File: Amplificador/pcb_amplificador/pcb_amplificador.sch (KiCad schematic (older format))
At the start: 102 parts, among them M1 FDS9934C, M2 FDS9934C, Q1 BC860, Q10 2SCR514P5, Q11 2SAR514P5, Q12 2SCR514P5, Q13 2SA1943-O_Q_, Q14 2SC5200-O_Q, Q15 2SA1943-O_Q_, Q16 2SC5200-O_Q, Q17 2SAR514P5, Q18 BC860, Q19 BC860, Q2 BC860, Q20 2SAR514P5, Q21 2SCR514P5, Q22 2SCR514P5, Q23 2SCR514P5, Q24 2SAR514P5, Q25 2SCR514P5, Q3 BC850, Q4 BC850, Q5 BC860, Q6 BC860, Q7 2SCR514P5, Q8 2SCR514P5, Q9 2SCR514P5

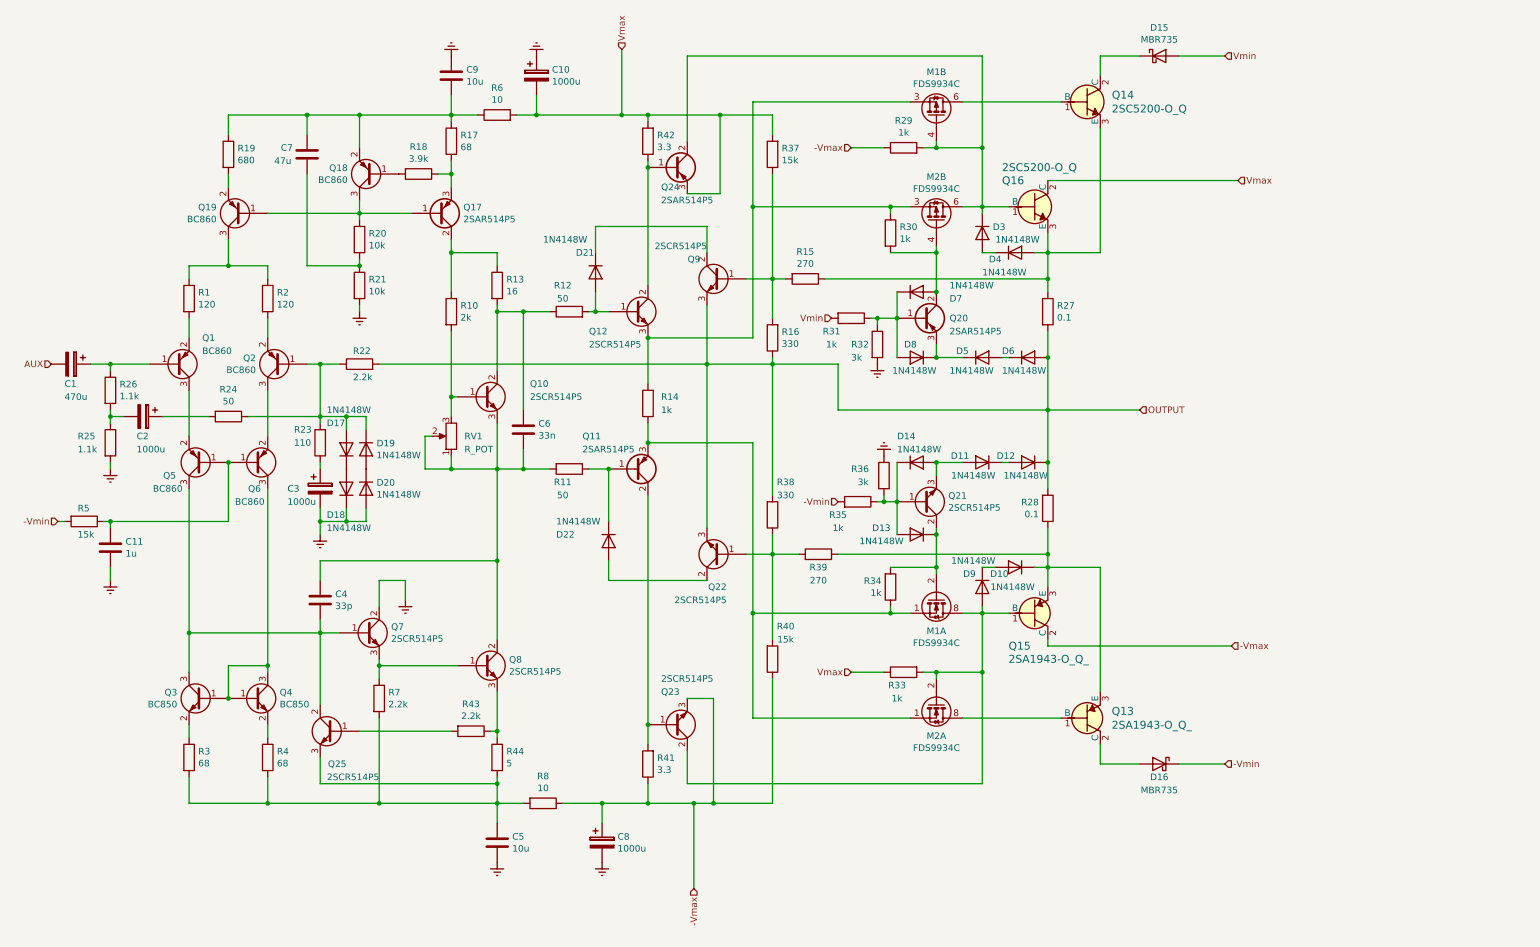
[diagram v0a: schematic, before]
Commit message: Actualizacion del esquematico del amplificador
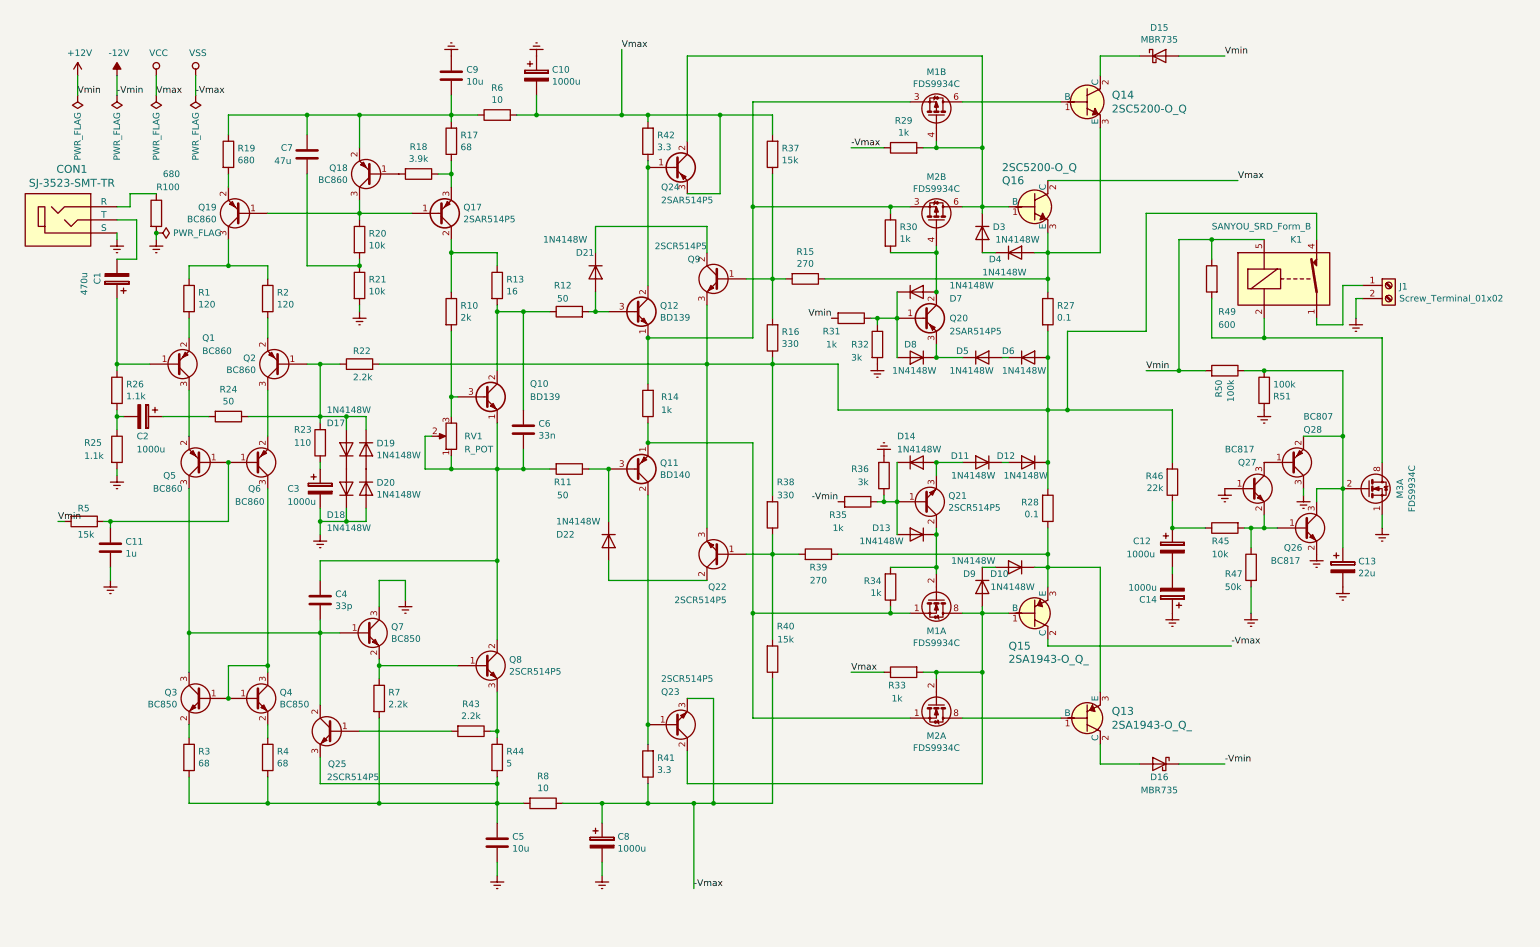
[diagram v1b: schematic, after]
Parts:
- removed Q10, Q12, Q7: 2SCR514P5, Package_TO_SOT_SMD:SOT-89-3, symbol amplificador_transistores:2SCR514P5
- removed Q11: 2SAR514P5, Package_TO_SOT_SMD:SOT-89-3, symbol amplificador_transistores:2SAR514P5
- added C12, C14: 1000u, symbol Device:CP
- added C13: 22u, symbol Device:CP
- added CON1: SJ-3523-SMT-TR, digikey-footprints:Switch_Slide_11.6x4mm_SJ-3523-SMT, symbol dk_Barrel-Audio-Connectors:SJ-3523-SMT-TR
- added J1: Screw_Terminal_01x02, symbol Connector:Screw_Terminal_01x02
- added K1: SANYOU_SRD_Form_B, Relay_THT:Relay_SPST_SANYOU_SRD_Series_Form_B, symbol Relay:SANYOU_SRD_Form_B
- added M3: FDS9934C, Package_SO:SOIC-8_3.9x4.9mm_P1.27mm, symbol Transistor_FET:FDS9934C
- added Q10, Q12: BD139, Package_TO_SOT_THT:TO-126-3_Vertical, symbol Transistor_BJT:BD139
- added Q11: BD140, Package_TO_SOT_THT:TO-126-3_Vertical, symbol Transistor_BJT:BD140
- added Q26, Q27: BC817, Package_TO_SOT_SMD:SOT-23, symbol Transistor_BJT:BC817
- added Q28: BC807, Package_TO_SOT_SMD:SOT-23, symbol Transistor_BJT:BC807
- added Q7: BC850, Package_TO_SOT_SMD:SOT-23, symbol Transistor_BJT:BC850
- added R100: 680, Resistor_SMD:R_0805_2012Metric_Pad1.15x1.40mm_HandSolder, symbol Device:R
- added R45: 10k, Resistor_SMD:R_0805_2012Metric_Pad1.15x1.40mm_HandSolder, symbol Device:R
- added R46: 22k, Resistor_SMD:R_0805_2012Metric_Pad1.15x1.40mm_HandSolder, symbol Device:R
- added R47: 50k, Resistor_SMD:R_0805_2012Metric_Pad1.15x1.40mm_HandSolder, symbol Device:R
- added R49: 600, Resistor_SMD:R_0805_2012Metric_Pad1.15x1.40mm_HandSolder, symbol Device:R
- added R50, R51: 100k, Resistor_SMD:R_0805_2012Metric_Pad1.15x1.40mm_HandSolder, symbol Device:R
- C4, C6: footprint (none) -> Capacitor_SMD:C_0805_2012Metric_Pad1.15x1.40mm_HandSolder
- R1, R10, R11, R12, R13, R14, R15, R16, R17, R18, R19, R2, R20, R22, R23, R24, R25, R26, R29, R3, R30, R31, R32, R33, R34, R35, R36, R37, R38, R39, R4, R40, R41, R42, R43, R44, R5, R6, R7, R8: footprint (none) -> Resistor_SMD:R_0805_2012Metric_Pad1.15x1.40mm_HandSolder
- R21: footprint (none) -> Resistor_SMD:R_0815_2038Metric_Pad1.53x4.00mm_HandSolder
- RV1: footprint (none) -> Potentiometer_THT:Potentiometer_Bourns_3296W_Vertical
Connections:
- net Earth: now also C13.2, C14.1, CON1.1 (S), J1.2 (Pin_2), M3.1 (S), Q26.2 (E), Q27.1 (B), Q28.3 (C), Q7.3 (C), R100.2, R47.2, R51.2
- net at C4.2, Q25.2 (C), Q3.3 (C)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: now also Q7.1 (B)
- net at Q8.1 (B), R7.1: now also Q7.2 (E)
- net at C4.1, C6.1, Q8.2 (C)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: now also Q10.1 (E)
- net at R10.2, RV1.3: now also Q10.3 (B)
- net at D22.1 (K), R11.1: now also Q11.3 (B)
- net at C6.2, R12.1, R13.2: now also Q10.2 (C)
- net at D21.2 (A), R12.2: now also Q12.3 (B)
- net at Q24.1 (B), R42.1: now also Q12.2 (C)
- net at M1.3 (1), M2.3 (1), R14.2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: now also Q12.1 (E)
- net at M1.1 (S), M2.1 (S), R14.1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: now also Q11.1 (E)
- net at Q23.1 (B), R41.2: now also Q11.2 (C)
- net -Vmax renamed VSS
- net -Vmin renamed -12V
- net -12V: no longer R5.2
- net AUX: no longer names the net of C1.2
- net AUX: now also CON1.2 (T)
- net OUTPUT: no longer names the net of D12.1 (K), D6.2 (A), Q22.3 (E), Q9.3 (E), R16.1, R22.2, R27.2, R28.2, R38.2
- net OUTPUT: now also K1.4, R46.2
- net Vmax renamed VCC
- net Vmin renamed +12V
- net +12V: now also R5.2, K1.5, R49.1, R50.2
- new net: Q26.1 (B), Q27.2 (E), R45.2, R47.1
- new net: C13.1, M3.2 (G), Q26.3 (C), Q28.2 (E), R50.1, R51.1
- new net: Q27.3 (C), Q28.1 (B)
- new net: C12.1, R45.1, R46.1
- new net: C12.2, C14.2
- new net: K1.2, M3.7 (D), M3.8 (D), R49.2
- new net: J1.1 (Pin_1), K1.1
- new net: CON1.3 (R), R100.1
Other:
- moved on the sheet: C1, R25, R26

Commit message: Actualizacion del esquematico del amplificador(2)
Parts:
- C1: value 470u -> 47u; footprint (none) -> Capacitor_SMD:CP_Elec_5x5.4
- C10, C8: footprint (none) -> Capacitor_THT:CP_Radial_D12.5mm_P5.00mm
- C11: footprint (none) -> Capacitor_SMD:C_0805_2012Metric_Pad1.15x1.40mm_HandSolder
- C12, C14: value 1000u -> 47u; footprint (none) -> Capacitor_SMD:CP_Elec_6.3x5.4
- C13: footprint (none) -> Capacitor_SMD:CP_Elec_5x5.4
- C2: value 1000u -> 470u; footprint (none) -> Capacitor_SMD:CP_Elec_10x10.5
- C3: footprint (none) -> Capacitor_SMD:CP_Elec_10x10.5
- C5, C9: footprint (none) -> Capacitor_SMD:C_1206_3216Metric_Pad1.42x1.75mm_HandSolder
- C7: footprint (none) -> Capacitor_SMD:CP_Elec_6.3x5.4
- R27, R28: footprint (none) -> Resistor_THT:R_Axial_DIN0414_L11.9mm_D4.5mm_P20.32mm_Horizontal
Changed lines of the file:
@@
 F 0 "C11" H 1315 4596 50  0000 L CNN
 F 1 "1u" H 1315 4505 50  0000 L CNN
-F 2 "" H 1238 4400 50  0001 C CNN
+F 2 "Capacitor_SMD:C_0805_2012Metric_Pad1.15x1.40mm_HandSolder" H 1238 4400 50  0001 C CNN
 F 3 "~" H 1200 4550 50  0001 C CNN
 	1    1200 4550
@@
 F 0 "C7" H 2900 1500 50  0000 R CNN
 F 1 "47u" H 2950 1600 50  0000 R CNN
-F 2 "" H 2738 1400 50  0001 C CNN
+F 2 "Capacitor_SMD:CP_Elec_6.3x5.4" H 2738 1400 50  0001 C CNN
 F 3 "~" H 2700 1550 50  0001 C CNN
 	1    2700 1550
@@
 F 0 "C5" H 4265 6846 50  0000 L CNN
 F 1 "10u" H 4265 6755 50  0000 L CNN
-F 2 "" H 4188 6650 50  0001 C CNN
+F 2 "Capacitor_SMD:C_1206_3216Metric_Pad1.42x1.75mm_HandSolder" H 4188 6650 50  0001 C CNN
 F 3 "~" H 4150 6800 50  0001 C CNN
 	1    4150 6800
@@
 F 0 "C8" H 5068 6846 50  0000 L CNN
 F 1 "1000u" H 5068 6755 50  0000 L CNN
-F 2 "" H 4988 6650 50  0001 C CNN
+F 2 "Capacitor_THT:CP_Radial_D12.5mm_P5.00mm" H 4988 6650 50  0001 C CNN
 F 3 "~" H 4950 6800 50  0001 C CNN
 	1    4950 6800
@@
 F 0 "C9" H 3685 904 50  0000 R CNN
 F 1 "10u" H 3685 995 50  0000 R CNN
-F 2 "" H 3838 800 50  0001 C CNN
+F 2 "Capacitor_SMD:C_1206_3216Metric_Pad1.42x1.75mm_HandSolder" H 3838 800 50  0001 C CNN
 F 3 "~" H 3800 950 50  0001 C CNN
 	1    3800 950
@@
 F 0 "C10" H 4568 996 50  0000 L CNN
 F 1 "1000u" H 4568 905 50  0000 L CNN
-F 2 "" H 4488 800 50  0001 C CNN
+F 2 "Capacitor_THT:CP_Radial_D12.5mm_P5.00mm" H 4488 800 50  0001 C CNN
 F 3 "~" H 4450 950 50  0001 C CNN
 	1    4450 950
@@
 F 0 "R27" H 8420 2796 50  0000 L CNN
 F 1 "0.1" H 8420 2705 50  0000 L CNN
-F 2 "" V 8280 2750 50  0001 C CNN
+F 2 "Resistor_THT:R_Axial_DIN0414_L11.9mm_D4.5mm_P20.32mm_Horizontal" V 8280 2750 50  0001 C CNN
 F 3 "~" H 8350 2750 50  0001 C CNN
 	1    8350 2750
@@
 F 0 "R28" H 8281 4204 50  0000 R CNN
 F 1 "0.1" H 8281 4295 50  0000 R CNN
-F 2 "" V 8280 4250 50  0001 C CNN
+F 2 "Resistor_THT:R_Axial_DIN0414_L11.9mm_D4.5mm_P20.32mm_Horizontal" V 8280 4250 50  0001 C CNN
 F 3 "~" H 8350 4250 50  0001 C CNN
 	1    8350 4250
@@
 F 0 "C3" H 2550 4100 50  0000 L CNN
 F 1 "1000u" H 2550 4000 50  0000 L CNN
-F 2 "" H 2838 3950 50  0001 C CNN
+F 2 "Capacitor_SMD:CP_Elec_10x10.5" H 2838 3950 50  0001 C CNN
 F 3 "~" H 2800 4100 50  0001 C CNN
 	1    2800 4100
@@
 P 1450 3550
 F 0 "C2" V 1600 3500 50  0000 L CNN
-F 1 "1000u" V 1700 3500 50  0000 L CNN
-F 2 "" H 1488 3400 50  0001 C CNN
+F 1 "470u" V 1700 3500 50  0000 L CNN
+F 2 "Capacitor_SMD:CP_Elec_10x10.5" H 1488 3400 50  0001 C CNN
 F 3 "~" H 1450 3550 50  0001 C CNN
 	1    1450 3550
@@
 P 1250 2500
 F 0 "C1" V 1400 2450 50  0000 L CNN
-F 1 "470u" V 1500 2450 50  0000 L CNN
-F 2 "" H 1288 2350 50  0001 C CNN
+F 1 "47u" V 1500 2450 50  0000 L CNN
+F 2 "Capacitor_SMD:CP_Elec_5x5.4" H 1288 2350 50  0001 C CNN
 F 3 "~" H 1250 2500 50  0001 C CNN
 	1    1250 2500
@@
 P 9300 4550
 F 0 "C12" H 9000 4600 50  0000 L CNN
-F 1 "1000u" H 8950 4500 50  0000 L CNN
-F 2 "" H 9338 4400 50  0001 C CNN
+F 1 "47u" H 8950 4500 50  0000 L CNN
+F 2 "Capacitor_SMD:CP_Elec_6.3x5.4" H 9338 4400 50  0001 C CNN
 F 3 "~" H 9300 4550 50  0001 C CNN
 	1    9300 4550
@@
 P 9300 4900
 F 0 "C14" H 9418 4946 50  0000 L CNN
-F 1 "1000u" H 9418 4855 50  0000 L CNN
-F 2 "" H 9338 4750 50  0001 C CNN
+F 1 "47u" H 9418 4855 50  0000 L CNN
+F 2 "Capacitor_SMD:CP_Elec_6.3x5.4" H 9338 4750 50  0001 C CNN
 F 3 "~" H 9300 4900 50  0001 C CNN
 	1    9300 4900
@@
 F 0 "C13" H 10718 4746 50  0000 L CNN
 F 1 "22u" H 10718 4655 50  0000 L CNN
-F 2 "" H 10638 4550 50  0001 C CNN
+F 2 "Capacitor_SMD:CP_Elec_5x5.4" H 10638 4550 50  0001 C CNN
 F 3 "~" H 10600 4700 50  0001 C CNN
 	1    10600 4700

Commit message: Comienzo del diseño del PCB del amplificador
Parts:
- added J2: Conn_01x03_Male, Connector_PinHeader_2.54mm:PinHeader_1x03_P2.54mm_Vertical, symbol Connector:Conn_01x03_Male
- added J3: Screw_Terminal_01x06, Connector_Phoenix_MC:PhoenixContact_MCV_1,5_6-G-3.5_1x06_P3.50mm_Vertical, symbol Connector:Screw_Terminal_01x06
- added Rp1, Rp2: 0, Resistor_SMD:R_0805_2012Metric_Pad1.15x1.40mm_HandSolder, symbol Device:R
- J1: footprint (none) -> Connector_Phoenix_MC:PhoenixContact_MCV_1,5_2-G-3.5_1x02_P3.50mm_Vertical
- R27, R28: footprint Resistor_THT:R_Axial_DIN0414_L11.9mm_D4.5mm_P20.32mm_Horizontal -> Resistor_SMD:R_2512_6332Metric_Pad1.52x3.35mm_HandSolder
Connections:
- net Earth: now also J2.3 (Pin_3), J3.5 (Pin_5), J3.6 (Pin_6)
- net at C4.2, Q25.2 (C), Q3.3 (C)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: now also Rp1.2; no longer Q5.3 (C)
- net at Q3.1 (B), Q4.1 (B), Q4.3 (C): now also Rp2.2; no longer Q6.3 (C)
- net at C1.2, CON1.2 (T): now also J2.1 (Pin_1)
- net +12V renamed Vmin
- net Vmin: now also J3.1 (Pin_1)
- net -12V renamed -Vmin
- net -Vmin: now also J3.2 (Pin_2)
- net VCC renamed Vmax
- net Vmax: now also J3.3 (Pin_3)
- net VSS renamed -Vmax
- net -Vmax: now also J3.4 (Pin_4)
- new net: Q5.3 (C), Rp1.1
- new net: Q6.3 (C), Rp2.1
- no-connect marks 0 -> 1
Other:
- moved on the sheet: C1, CON1, R100

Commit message: Avance con el PCB
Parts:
- added R9: 0, Resistor_SMD:R_1206_3216Metric_Pad1.42x1.75mm_HandSolder, symbol Device:R
- K1: symbol Relay:SANYOU_SRD_Form_B -> pcb_amplificador-rescue:SANYOU_SRD_Form_B-Relay
- R21: footprint Resistor_SMD:R_0815_2038Metric_Pad1.53x4.00mm_HandSolder -> Resistor_SMD:R_0805_2012Metric_Pad1.15x1.40mm_HandSolder
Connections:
- net at C4.1, C6.1, Q10.1 (E)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: now also R9.1; no longer Q8.2 (C)
- new net: Q8.2 (C), R9.2
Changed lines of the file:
@@
 EESchema Schematic File Version 4
 LIBS:pcb_amplificador-cache
-EELAYER 29 0
+EELAYER 26 0
 EELAYER END
 $Descr A4 11693 8268
@@
 F 0 "R21" H 3170 2596 50  0000 L CNN
 F 1 "10k" H 3170 2505 50  0000 L CNN
-F 2 "Resistor_SMD:R_0815_2038Metric_Pad1.53x4.00mm_HandSolder" V 3030 2550 50  0001 C CNN
+F 2 "Resistor_SMD:R_0805_2012Metric_Pad1.15x1.40mm_HandSolder" V 3030 2550 50  0001 C CNN
 F 3 "~" H 3100 2550 50  0001 C CNN
 	1    3100 2550
@@
 Connection ~ 4150 4650
 Wire Wire Line
-	4150 4650 4150 5250
+	4150 4650 4150 4800
 Wire Wire Line
 	2800 5100 2800 5200
@@
 $EndComp
 $Comp
-L Relay:SANYOU_SRD_Form_B K1
+L pcb_amplificador-rescue:SANYOU_SRD_Form_B-Relay K1
 U 1 1 5D0A74B1
 P 10200 2500
@@
 Wire Wire Line
 	1050 2500 1050 3150
+$Comp
+L Device:R R9
+U 1 1 5D09C039
+P 4150 4950
+F 0 "R9" H 4220 4996 50  0000 L CNN
+F 1 "0" H 4220 4905 50  0000 L CNN
+F 2 "Resistor_SMD:R_1206_3216Metric_Pad1.42x1.75mm_HandSolder" V 4080 4950 50  0001 C CNN
+F 3 "~" H 4150 4950 50  0001 C CNN
+	1    4150 4950
+	1    0    0    -1
+$EndComp
+Wire Wire Line
+	4150 5100 4150 5250
 $EndSCHEMATC
